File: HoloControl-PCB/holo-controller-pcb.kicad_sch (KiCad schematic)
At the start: 35 parts, among them Q1 2N3904, Q2 2N3904, Q3 2N3904, Q4 2N3904, SW1 SW_DPDT_x2, SW2 SW_Push, SW3 SW_Push, U1 Pico

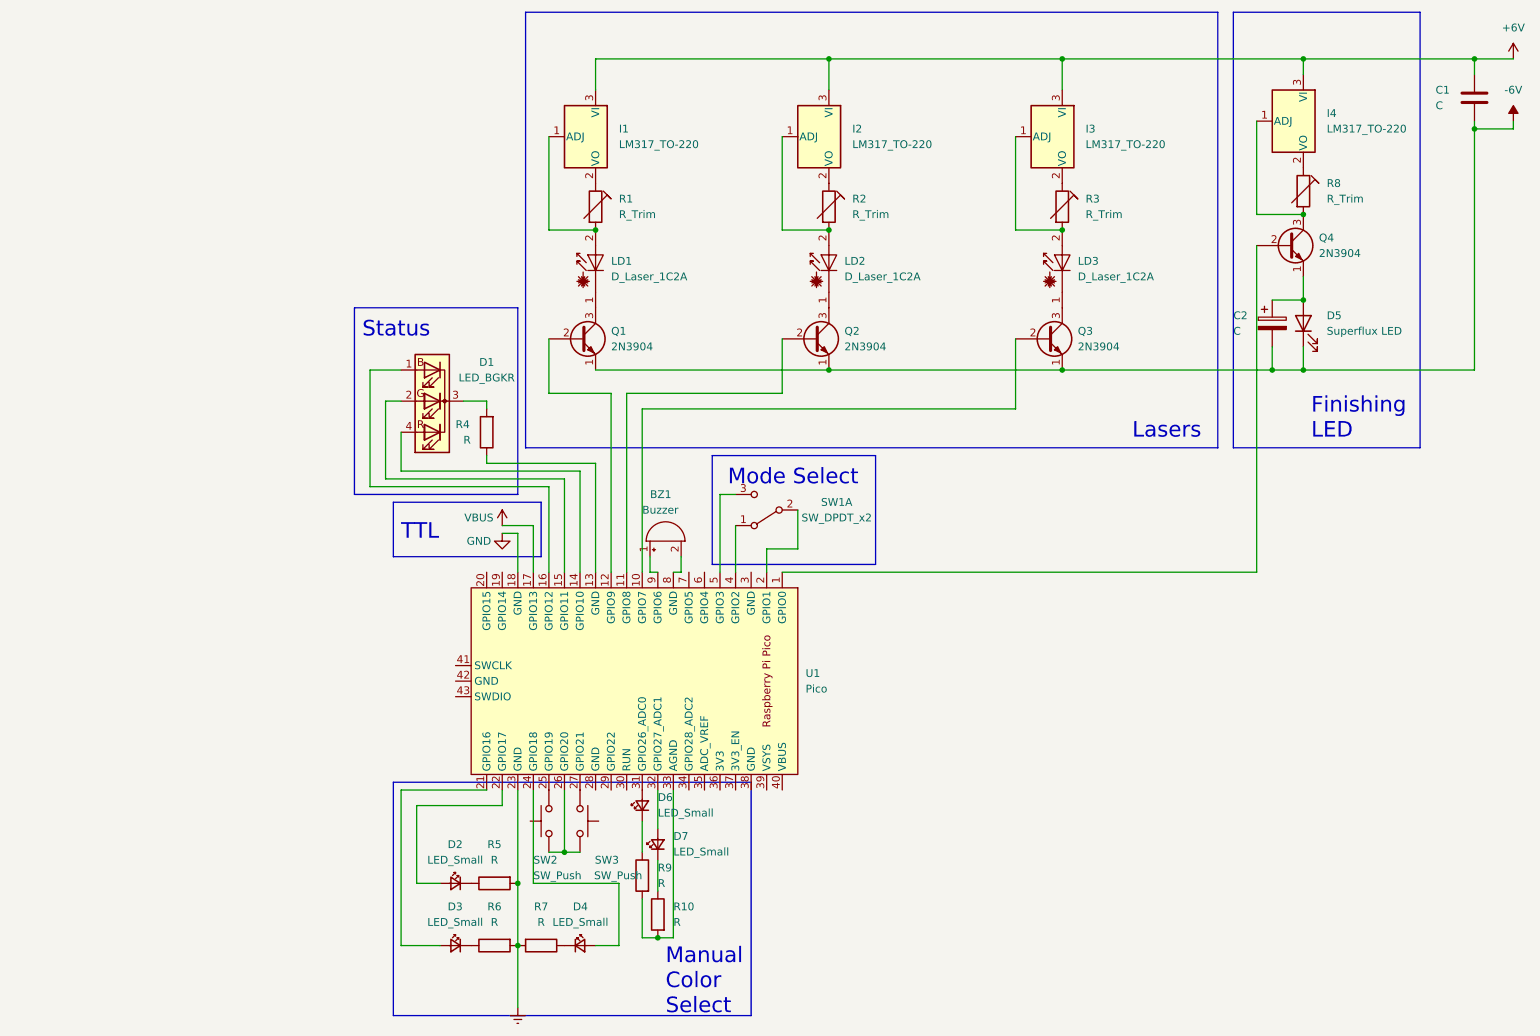
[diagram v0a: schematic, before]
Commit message: Update PCB schematic to new current regulator design
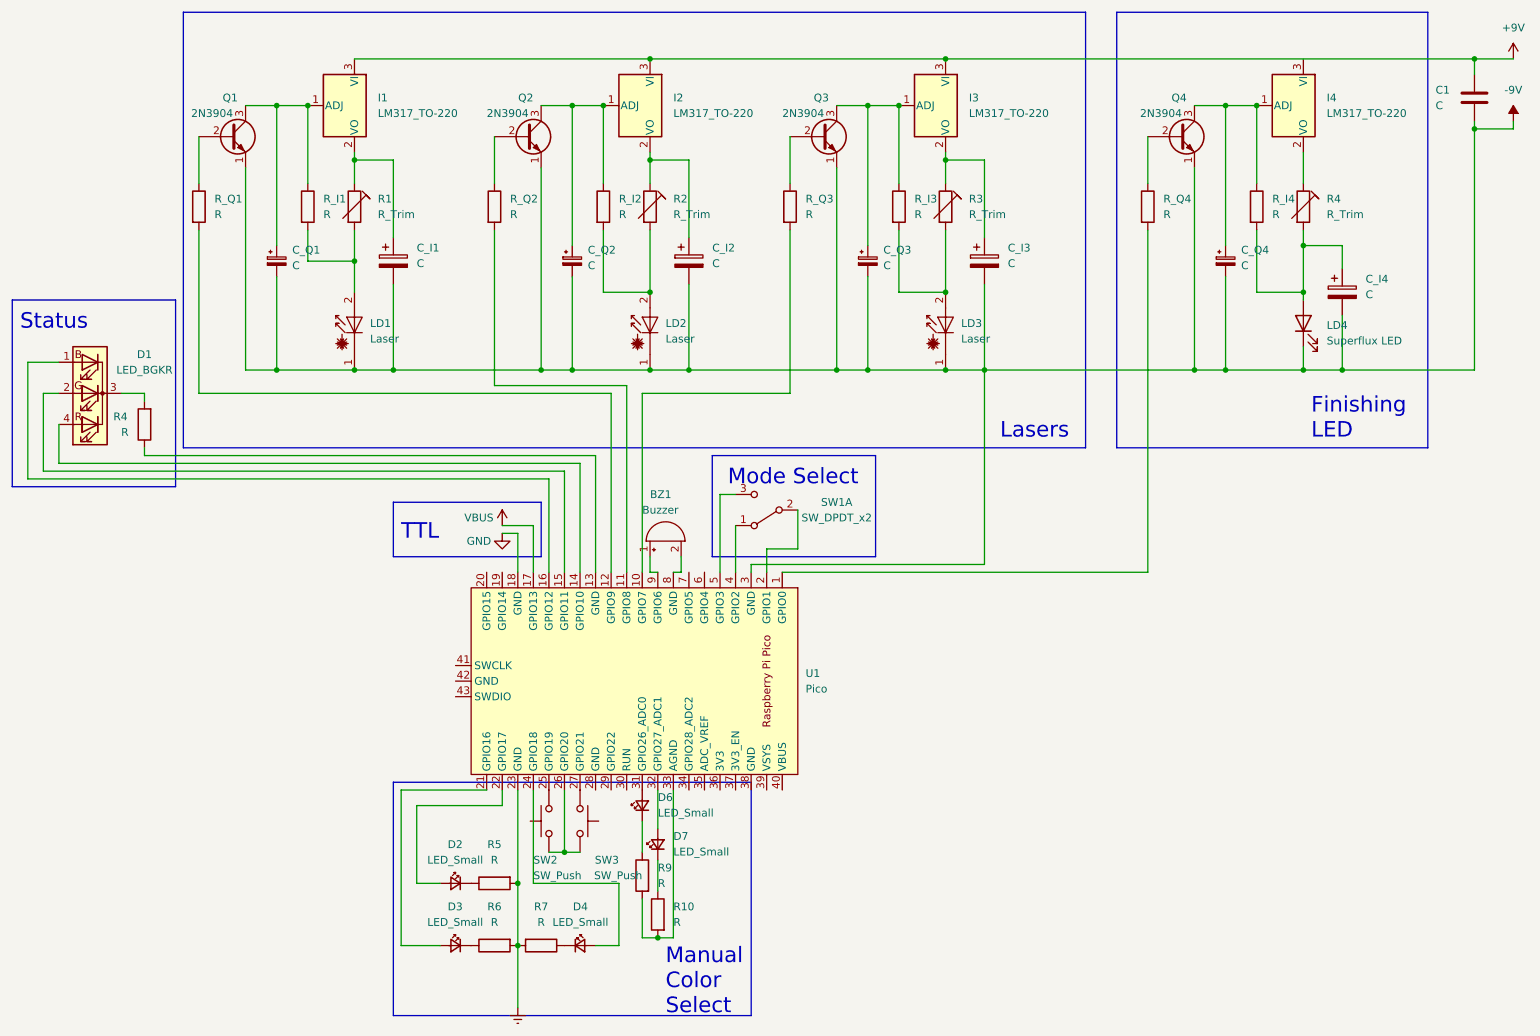
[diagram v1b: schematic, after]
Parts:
- removed C2: C, symbol Device:C_Polarized
- removed D5: Superflux LED, symbol Device:LED
- removed R8: R_Trim, symbol Device:R_Trim
- added C_I1, C_I2, C_I3, C_I4: C, symbol Device:C_Polarized
- added C_Q1, C_Q2, C_Q3, C_Q4: C, symbol Device:C_Polarized_Small
- added LD4: Superflux LED, symbol Device:LED
- added R4: R_Trim, symbol Device:R_Trim
- added R_I1, R_I2, R_I3, R_I4, R_Q1, R_Q2, R_Q3, R_Q4: R, symbol Device:R
- LD1, LD2, LD3: value D_Laser_1C2A -> Laser
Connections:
- net -6V is gone; now on net -9V: C1.2, Q1.1 (E), Q2.1 (E), Q3.1 (E)
- net at I3.2 (VO), R3.1: now also C_I3.1
- net at LD3.2 (A), R3.2: now also R_I3.2; no longer I3.1 (ADJ)
- net -9V: now reaches Q4.1 (E)
- net -9V: now also LD1.1 (K), LD2.1 (K), LD3.1 (K), U1.3 (GND), C_I1.2, C_I2.2, C_I3.2, C_I4.2, C_Q1.2, C_Q2.2, C_Q3.2, C_Q4.2, LD4.1 (K)
- net at Q4.2 (B): now also R_Q4.1; no longer U1.1 (GPIO0)
- net at I4.1 (ADJ), Q4.3 (C): now also C_Q4.1, R_I4.1
- net at I2.2 (VO), R2.1: now also C_I2.1
- net at LD2.2 (A), R2.2: now also R_I2.2; no longer I2.1 (ADJ)
- net at I4.2 (VO): now also R4.1
- net at Q2.2 (B): now also R_Q2.1; no longer U1.11 (GPIO8)
- net at Q2.3 (C): now also I2.1 (ADJ), C_Q2.1, R_I2.1; no longer LD2.1 (K)
- net at Q1.3 (C): now also I1.1 (ADJ), C_Q1.1, R_I1.1; no longer LD1.1 (K)
- net at LD1.2 (A), R1.2: now also R_I1.2; no longer I1.1 (ADJ)
- net at I1.2 (VO), R1.1: now also C_I1.1
- net at Q3.2 (B): now also R_Q3.1; no longer U1.10 (GPIO7)
- net at Q3.3 (C): now also I3.1 (ADJ), C_Q3.1, R_I3.1; no longer LD3.1 (K)
- net at Q1.2 (B): now also R_Q1.1; no longer U1.12 (GPIO9)
- net +6V renamed +9V
- net +9V: no longer I4.3 (VI)
- new net: R_Q1.2, U1.12 (GPIO9)
- new net: C_I4.1, LD4.2 (A), R4.2, R_I4.2
- new net: R_Q2.2, U1.11 (GPIO8)
- new net: R_Q3.2, U1.10 (GPIO7)
- new net: R_Q4.2, U1.1 (GPIO0)
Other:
- moved on the sheet: D1, I1, LD1, Q1, R1, R4

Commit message: Update board - Includes a change to pinout of white LEDs (swapped)
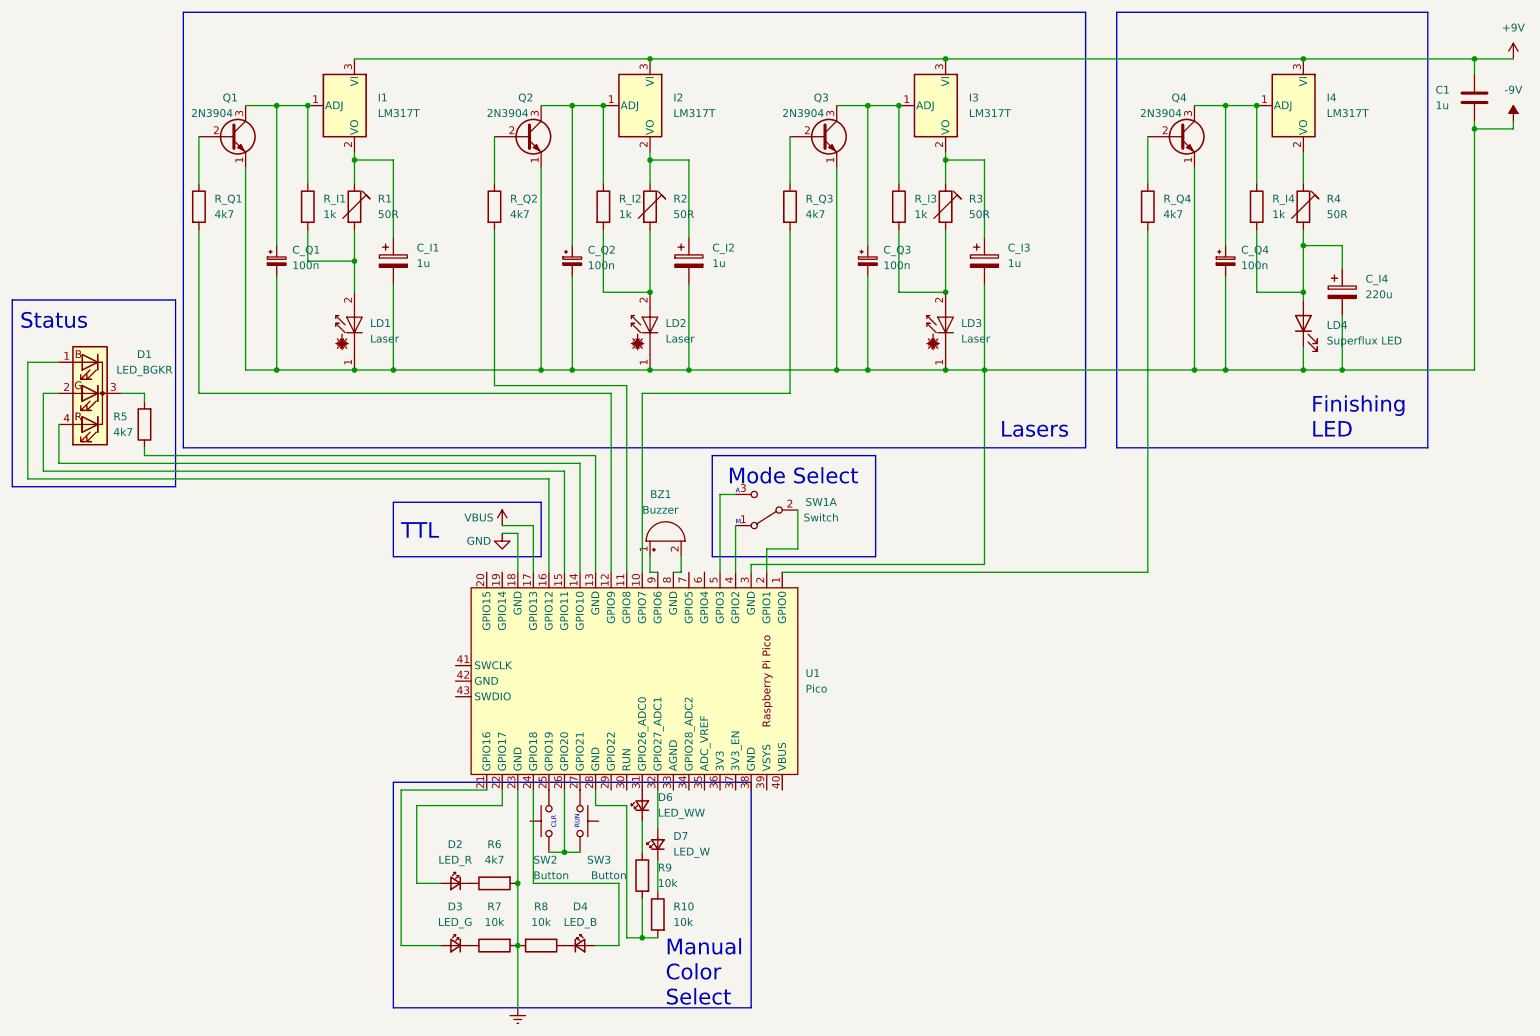
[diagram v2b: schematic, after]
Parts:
- C1, C_I1, C_I2, C_I3: value C -> 1u
- C_I4: value C -> 220u
- C_Q1, C_Q2, C_Q3, C_Q4: value C -> 100n
- D2: value LED_Small -> LED_R
- D3: value LED_Small -> LED_G
- D4: value LED_Small -> LED_B
- D6: value LED_Small -> LED_WW
- D7: value LED_Small -> LED_W
- I1, I2, I3, I4: value LM317_TO-220 -> LM317T
- R1, R2, R3, R4: value R_Trim -> 50R
- R10, R9: value R -> 10k
- R5: renamed from R4; value R -> 4k7
- R6: renamed from R5; value R -> 4k7
- R7: renamed from R6; value R -> 10k
- R8: renamed from R7; value R -> 10k
- R_I1, R_I2, R_I3, R_I4: value R -> 1k
- R_Q1, R_Q2, R_Q3, R_Q4: value R -> 4k7
- SW1: value SW_DPDT_x2 -> Switch
- SW2, SW3: value SW_Push -> Button
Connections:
- net +9V: now also I4.3 (VI)
- net at R10.2, R9.2: now also U1.28 (GND); no longer U1.33 (AGND)
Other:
- note added: "A"
- note added: "CLR"
- note added: "M"
- note added: "RUN"
